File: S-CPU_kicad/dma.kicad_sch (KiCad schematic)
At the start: 31 parts, among them U1 NAND_2, U10 NAND_2, U11 INVERTER_A, U12 INVERTER_A, U13 INVERTER_A, U14 INVERTER_A, U15 NOR_2, U16 DFFR_B, U17 OR_2, U18 NAND_2, U19 DFFR_B, U2 NAND_2, U20 DFFR_B, U21 DFFR_B, U22 NAND_4, U23 NAND_2, U24 INVERTER_A, U25 OR_3, U26 NAND_4, U27 NOR_3, U29 NAND_2, U3 NAND_2, U30 NAND_5, U31 NOR_3, U32 NAND_2, U34 INVERTER_A, U35 NAND_2, U4 NAND_2, U5 NAND_2, U7 NAND_2, U9 NAND_2

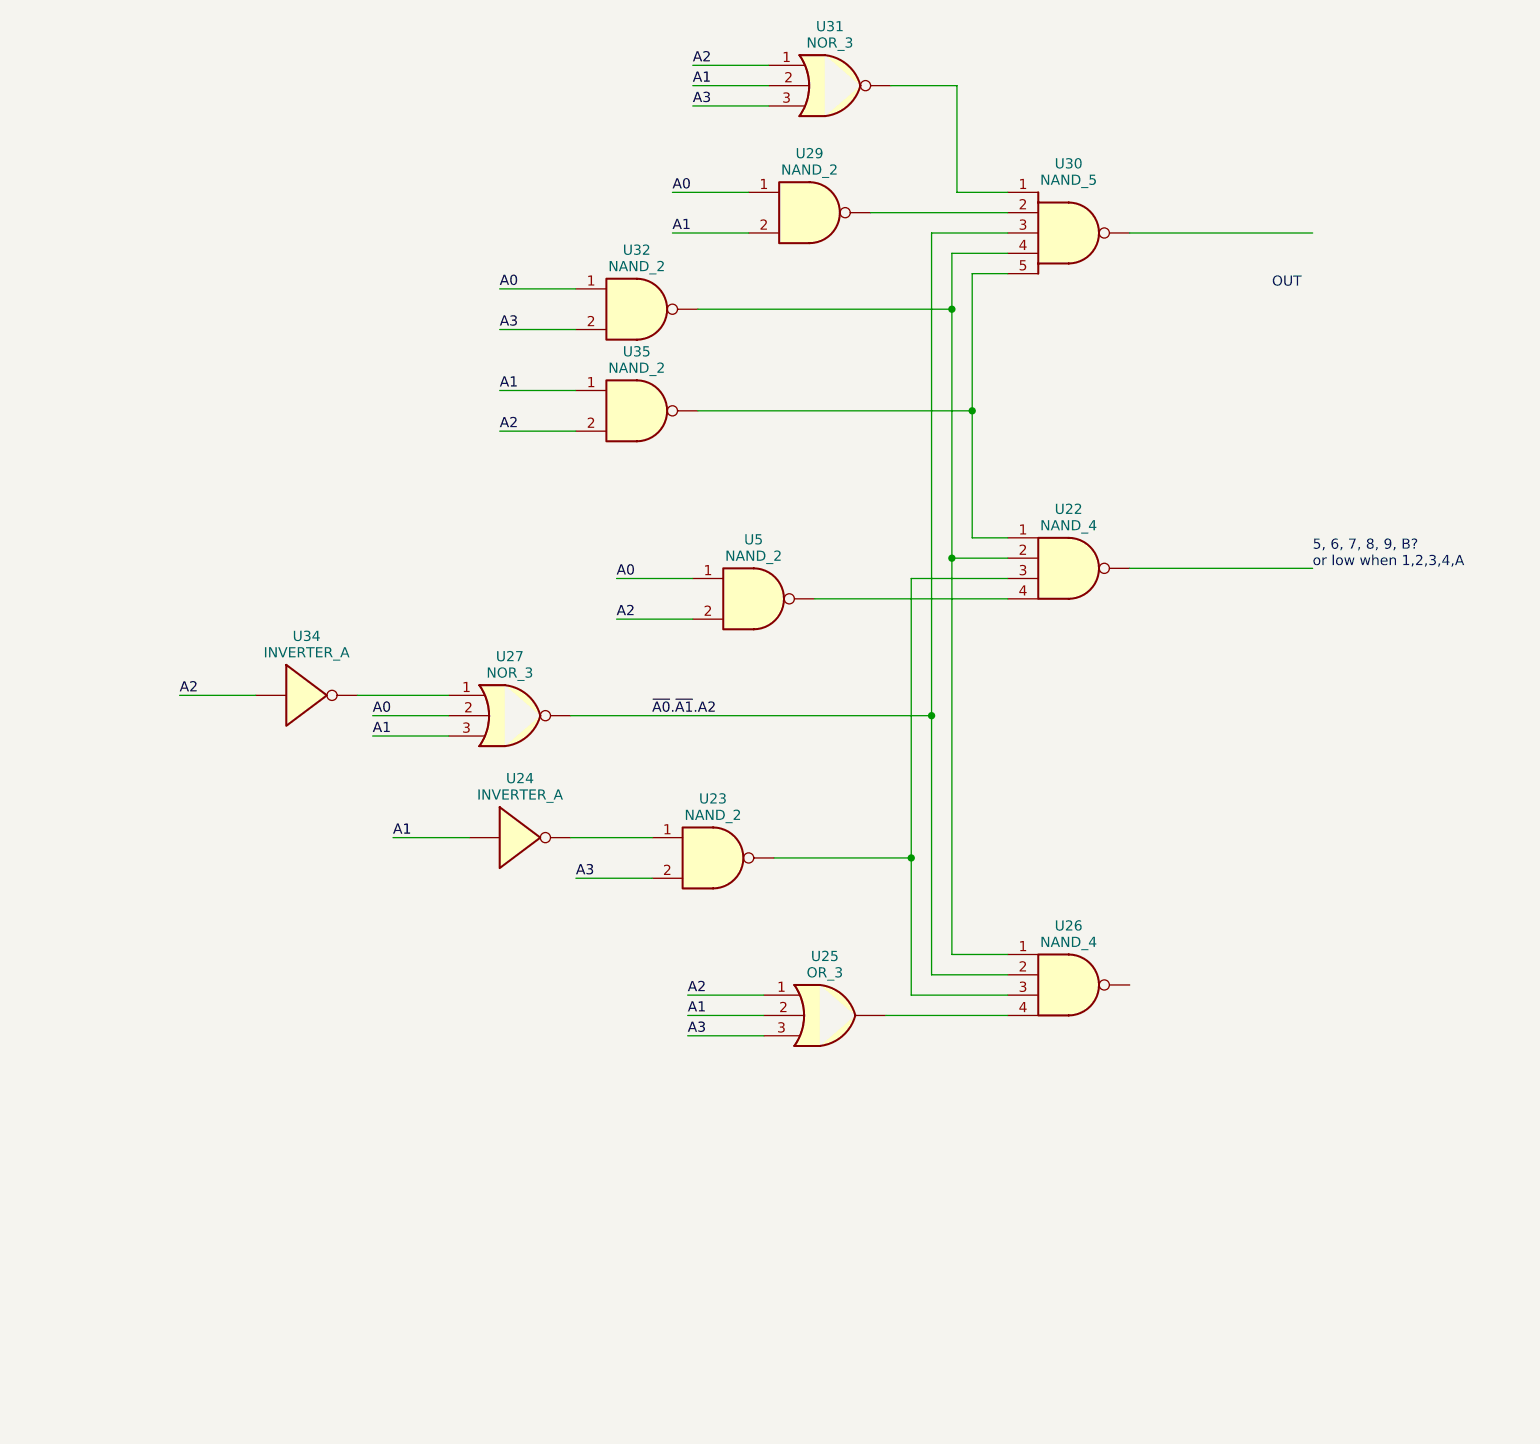
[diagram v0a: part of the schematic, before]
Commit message: Some cells had the wrong ID in the producter remainder sheet. Allocation of new names in spreadsheet for cells in the DMA section
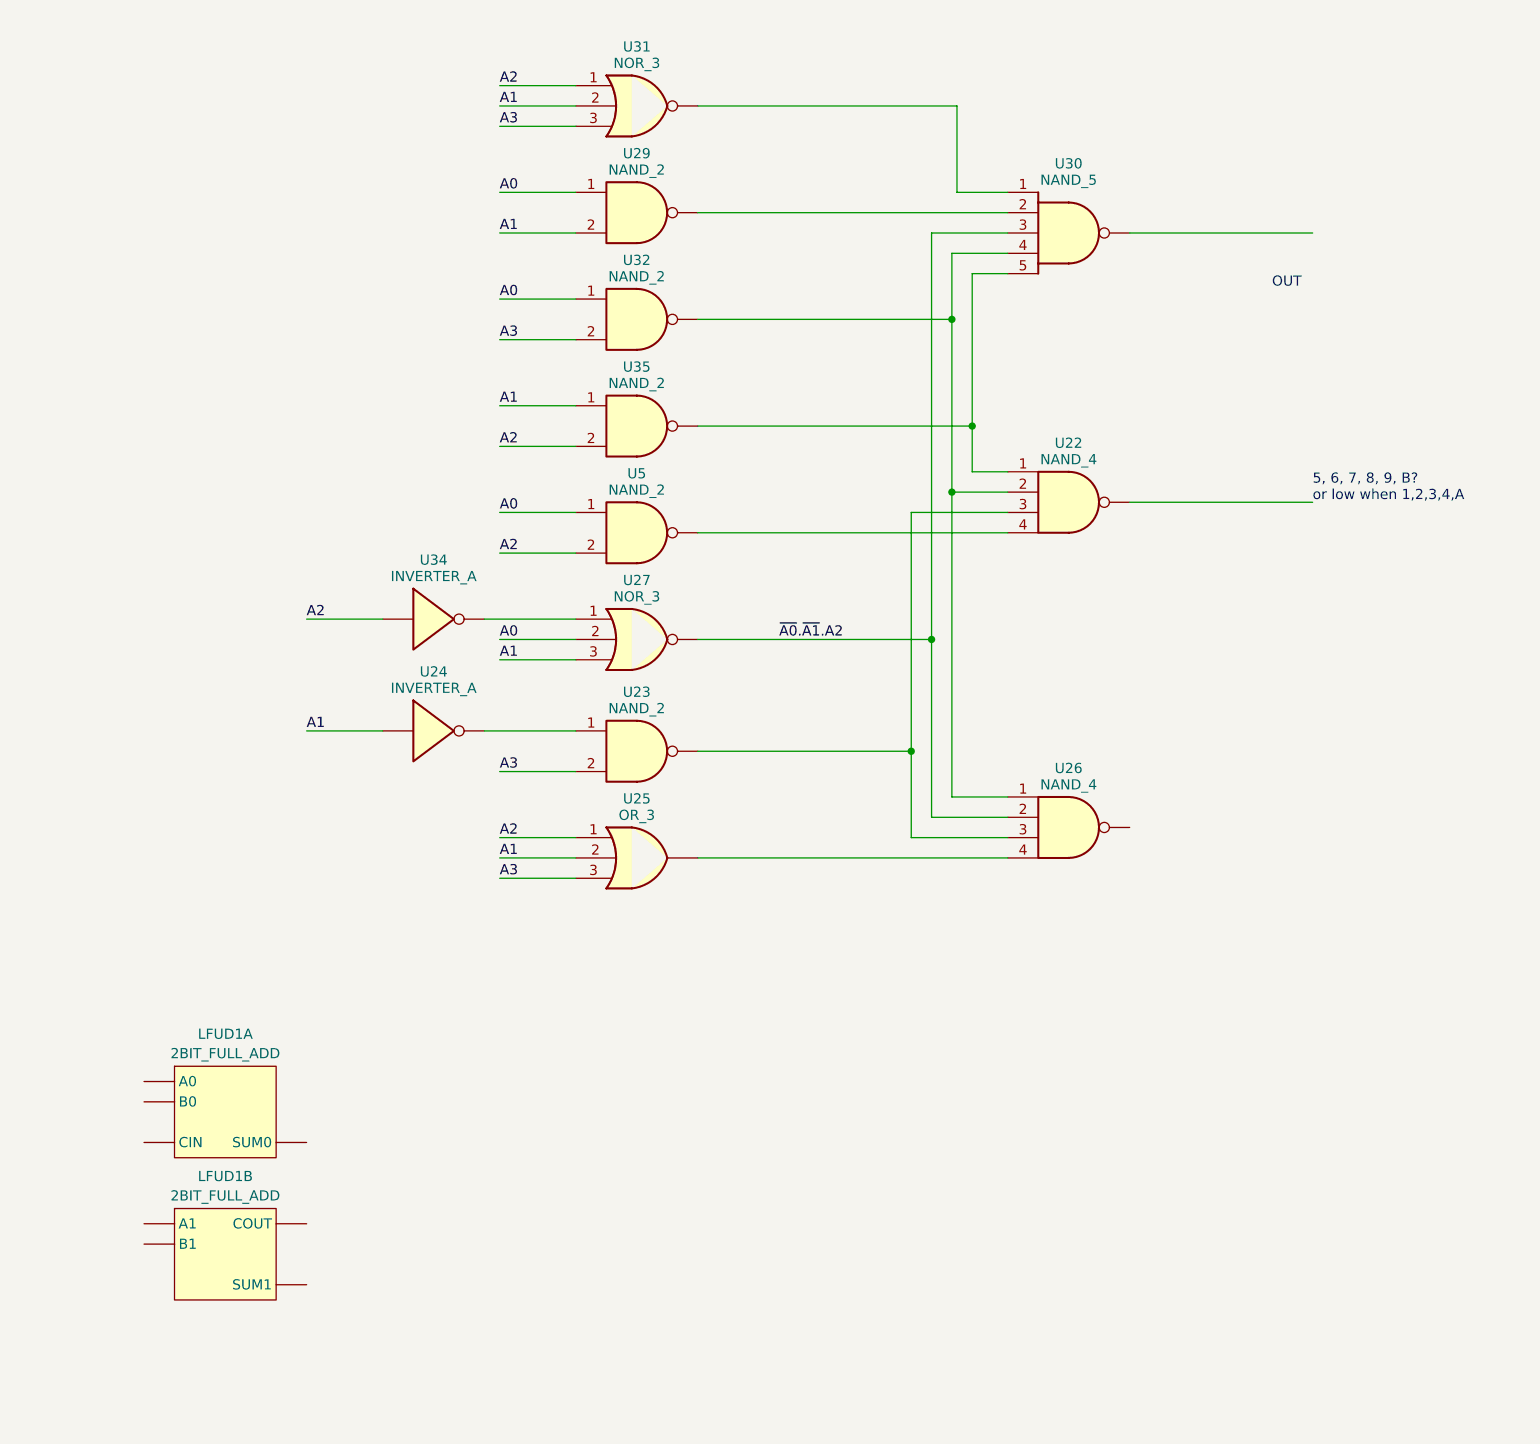
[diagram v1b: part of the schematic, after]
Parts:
- added LFUD1: 2BIT_FULL_ADD, symbol Ricoh_Cells:2BIT_FULL_ADD
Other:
- moved on the sheet: U22, U23, U24, U25, U26, U27, U29, U31, U32, U34, U35, U5

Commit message: Bit DMA section update. Untangled a lot of singals. DMA addressing decoding worked out + connections to DMA RAM.
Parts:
- added AMCK, AMQL: NAND_4, symbol Ricoh_Cells:NAND_4
- added AMEV, AMGY, ANAY, U23, U26, U5: NAND_2, symbol Ricoh_Cells:NAND_2
- added AMEX, AMLH, OKHF (x2), OKPW, OKSL, OKUR, OLCW, OLHT, OLMD, OLOZ, OLRW, OLUQ, OLWK, OMDX, OMMV, QKAT, QKGG, QKLR, RKPQ, RKPR, RKRK, SKPA, TKAS, U22, U24, U25, U27, YKBE: INVERTER_A, symbol Ricoh_Cells:INVERTER_A
- added AMMZ, TKAT: NOR_3, symbol Ricoh_Cells:NOR_3
- added AMZL, DMA?, SKKT, TKAY, TKHG, ULGF, VKDC, VKDV, VKEQ, XKIN, YKCI, YKDI, YKFE, YKHM, YKJS, YKMK: OR_2, symbol Ricoh_Cells:OR_2
- added DMA_RAM_BANK0, DMA_RAM_BANK1, DMA_RAM_BANK2: DMA_RAM, symbol Ricoh_Cells:DMA_RAM
- added EBSG (x2), EBVQ (x2), EBXE (x2), EBYP (x2), ECCU (x2), ECEK (x2), ECGN (x2), ECGO (x2), QKBI, RKNG, SKDA, UKGM, UKGO, UKHI, UKHP, UKOH, UKWD, UKYL (x2): DFFR_A, symbol Ricoh_Cells:DFFR_A
- added OKMN0, OKMN1, OKMN2, OKMN3, OKTR0, OKTR1, OKTR2, OKTR3, OKTY0, OKTY1, OKTY2, OKTY3, OLCO0, OLCO1, OLCO2, OLCO3, OLDU0, OLDU1, OLDU2, OLDU3, OLGV0, OLGV1, OLGV2, OLGV3, OLNC0, OLNC1, OLNC2, OLNC3, OLSH0, OLSH1, OLSH2, OLSH3, OLWI0, OLWI1, OLWI2, OLWI3, OLXX0, OLXX1, OLXX2, OLXX3, OMIG0, OMIG1, OMIG2, OMIG3, OMNC0, OMNC1, OMNC2, OMNC3, QKEL0, QKEL1, QKEL2, QKEL3, QKQM0, QKQM1, QKQM2, QKQM3, RKOE0, RKOE1, RKOE2, RKOE3, RKUL0, RKUL1, RKUL2, RKUL3: TRI_BUF_IF1, symbol Ricoh_Cells:TRI_BUF_IF1
- added OKWN, OLYU, OLZN, OMBB, PKBG, PKEJ, QKAI, SKJF: BUF_DIFF, symbol Ricoh_Cells:BUF_DIFF
- added OLCL0, OLCL1, OLCL2, OLCL3, OLCL4, OLCL5, OLCL6, OLCL7, OLYP0, OLYP1, OLYP2, OLYP3, OLYP4, OLYP5, OLYP6, OLYP7, OLZR0, OLZR1, OLZR2, OLZR3, OLZR4, OLZR5, OLZR6, OLZR7, OMDK0, OMDK1, OMDK2, OMDK3, OMDK4, OMDK5, OMDK6, OMDK7, PKBB0, PKBB1, PKBB2, PKBB3, PKBB4, PKBB5, PKBB6, PKBB7, PKEM0, PKEM1, PKEM2, PKEM3, PKEM4, PKEM5, PKEM6, PKEM7, QKAG0, QKAG1, QKAG2, QKAG3, QKAG4, QKAG5, QKAG6, SKKP0, SKKP1, SKKP2, SKKP3, SKKP4, SKKP5, SKKP6, SKKP7: D_LATCH_ARRAY, symbol Ricoh_Cells:D_LATCH_ARRAY
- added QKAG7, QKAG8, QKAG9, TKGB: DFFR_B, symbol Ricoh_Cells:DFFR_B
- added QKCI, RKMD, RKNZ, SKCS, SKHI, TKBH, TKFI, TKFN, UKZF, ULBK, VKID, VKJK: 2BIT_FULL_ADD, symbol Ricoh_Cells:2BIT_FULL_ADD
- added QKHU, RKQY: NAND_3, symbol Ricoh_Cells:NAND_3
- added RKLP, SKCM, TKIB, TKIB?, U28: AND_2, symbol Ricoh_Cells:AND_2
- added TKDG, WKCF, WKNO, XKGP, XKKB, XKKC, XKKE: OR_3, symbol Ricoh_Cells:OR_3
- added UBNH: NAND_5, symbol Ricoh_Cells:NAND_5
- added VKBO, VKCI, XKBP, XKDB: MUX_2x4:1, symbol Ricoh_Cells:MUX_2x4{colon}1
- added WKSN, WKZC, XKIG, XKQM, YKAW, YKBC, ZKBA, ZKBW: MUX_4x2:1, symbol Ricoh_Cells:MUX_4x2{colon}1
- BNBV: renamed from U31; value NOR_3 -> OR_3; symbol Ricoh_Cells:NOR_3 -> Ricoh_Cells:OR_3
- BNLF: renamed from U27; value NOR_3 -> OR_3; symbol Ricoh_Cells:NOR_3 -> Ricoh_Cells:OR_3
- renumbered U29 to BNAP, U30 to BNHI, U34 to BNNS, U32 to BNOQ, U26 to BNVB, U35 to BNXG, U22 to BNYC, U5 to SKQJ, U24 to ULHH, U23 to ULHM, U25 to VKJX
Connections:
- net A0: now also AMEX.1, AMGY.2, AMMZ.3, AMZL.1, OKHF.1, OKTR3.4, QKQM0.1 (IN), QKQM0.3 (IN)
- net A1: now also AMEV.1, AMLH.1, AMZL.2, ANAY.1, OKHF.1, OKTR2.4, QKQM1.1 (IN), QKQM1.3 (IN); no longer VKJX.2
- net A2: now also AMMZ.2, OKTR1.4, QKQM2.1 (IN), QKQM2.3 (IN), UBNH.2
- net A3: now also ANAY.2, OKTR0.4, QKQM3.1 (IN), QKQM3.3 (IN), UBNH.3
- net at BNVB.3, BNYC.3, ULHM.3: now also AMCK.4
- net ~{A1}+A2+A3: now reaches BNVB.4, VKJX.4
- net at BNVB.5: now also ZKBA.5
- net at ULHH.2, ULHM.1: now also VKJX.2
- net A1+A2+A3: now reaches BNBV.4, BNHI.1
- net at BNHI.6: now also YKCI.2
- net at BNYC.4, SKQJ.3: now also AMCK.3, AMQL.2
- net at BNYC.5: now also ZKBA.13
- net ~{A0}.~{A1}.A2 renamed A0+A1+~{A2}
- new net: RKMD.28 (COUT), SKCS.2 (CIN)
- new net: OLYP2.4 (Q), SKCS.9 (B0)
- new net: VKBO.24, YKAW.13
- new net: OLUQ.2, OLWI0.2 (~{ENA}), OLWI1.2 (~{ENA}), OLWI2.2 (~{ENA}), OLWI3.2 (~{ENA})
- new net: WKZC.7, XKQM.5
- new net: UKHP.1 (~{RESET}), UKHP.5 (~{RESET})
- new net: UKGM.3 (CLK), UKGM.4 (~{CLK}), UKGO.3 (CLK), UKGO.4 (~{CLK}), UKHI.3 (CLK), UKHI.4 (~{CLK}), UKHP.3 (CLK), UKHP.4 (~{CLK}), UKOH.3 (CLK), UKOH.4 (~{CLK}), UKWD.3 (CLK), UKWD.4 (~{CLK}), UKYL.3 (CLK), UKYL.3 (CLK), UKYL.4 (~{CLK}), UKYL.4 (~{CLK}), ULGF.3
- new net: UKHP.6 (Q), VKCI.11
- new net: AMGY.1, AMLH.2, AMMZ.1
- new net: OLGV1.1 (IN), OLGV1.3 (IN)
- new net: OLGV0.2 (~{ENA}), OLGV1.2 (~{ENA}), OLGV2.2 (~{ENA}), OLGV3.2 (~{ENA}), OLHT.2
- new net: RKUL0.1 (IN), RKUL0.3 (IN), SKKP4.4 (Q)
- new net: RKRK.2, RKUL0.2 (~{ENA}), RKUL1.2 (~{ENA}), RKUL2.2 (~{ENA}), RKUL3.2 (~{ENA})
- new net: UKYL.6 (Q), XKBP.11
- new net: EBXE.6 (Q), XKBP.14
- new net: XKBP.24, YKBC.13
- new net: UKGO.1 (~{RESET}), UKGO.5 (~{RESET})
- new net: UKGO.6 (Q), VKBO.11
- new net: UKZF.13 (A0), UKZF.24 (A1), ULBK.13 (A0), ULBK.24 (A1), VKID.13 (A0), VKID.24 (A1), VKJK.13 (A0), VKJK.24 (A1)
- new net: UKZF.28 (COUT), ULBK.2 (CIN)
- new net: OLZR6.4 (Q), ULBK.9 (B0)
- new net: WKCF.4, WKNO.3
- new net: UKZF.2 (CIN), VKJK.28 (COUT)
- new net: OLZR4.4 (Q), UKZF.9 (B0)
- new net: VKCI.24, YKAW.25
- new net: OLYP0.1 (~{ENA}), OLYP1.1 (~{ENA}), OLYP2.1 (~{ENA}), OLYP3.1 (~{ENA}), OLYP4.1 (~{ENA}), OLYP5.1 (~{ENA}), OLYP6.1 (~{ENA}), OLYP7.1 (~{ENA}), OLYU.2
- new net: OLYP0.3 (ENA), OLYP1.3 (ENA), OLYP2.3 (ENA), OLYP3.3 (ENA), OLYP4.3 (ENA), OLYP5.3 (ENA), OLYP6.3 (ENA), OLYP7.3 (ENA), OLYU.2
- new net: OLYP1.4 (Q), RKMD.23 (B1)
- new net: RKUL1.1 (IN), RKUL1.3 (IN), SKKP5.4 (Q)
- new net: OMBB.2, OMDK0.1 (~{ENA}), OMDK1.1 (~{ENA}), OMDK2.1 (~{ENA}), OMDK3.1 (~{ENA}), OMDK4.1 (~{ENA}), OMDK5.1 (~{ENA}), OMDK6.1 (~{ENA}), OMDK7.1 (~{ENA})
- new net: OMBB.2, OMDK0.3 (ENA), OMDK1.3 (ENA), OMDK2.3 (ENA), OMDK3.3 (ENA), OMDK4.3 (ENA), OMDK5.3 (ENA), OMDK6.3 (ENA), OMDK7.3 (ENA)
- new net: OMDK2.4 (Q), TKFN.9 (B0)
- new net: U26.1, U27.2
- new net: U26.3, U28.1
- new net: TKGB.6 (~{Q}), TKHG.1
- new net: TKHG.3, TKIB.2
- new net: SKDA.1 (~{RESET}), SKDA.5 (~{RESET})
- new net: QKAG1.4 (Q), SKDA.2 (D)
- new net: QKAT.2, QKBI.3 (CLK), QKBI.4 (~{CLK}), RKNG.3 (CLK), RKNG.4 (~{CLK}), SKDA.3 (CLK), SKDA.4 (~{CLK})
- new net: OKTY0.2 (~{ENA}), OKTY1.2 (~{ENA}), OKTY2.2 (~{ENA}), OKTY3.2 (~{ENA}), OKUR.2
- new net: OMDK6.4 (Q), RKNZ.9 (B0)
- new net: XKKC.1, XKKE.4
- new net: VKBO.1 (SEL0), VKCI.1 (SEL0), WKSN.1 (SEL), WKZC.1 (SEL), XKBP.1 (SEL0), XKDB.1 (SEL0), XKIG.1 (SEL), XKQM.1 (SEL), YKAW.1 (SEL), YKBC.1 (SEL), YKBE.2, ZKBA.1 (SEL), ZKBW.1 (SEL)
- new net: PKEJ.2, PKEM0.1 (~{ENA}), PKEM1.1 (~{ENA}), PKEM2.1 (~{ENA}), PKEM3.1 (~{ENA}), PKEM4.1 (~{ENA}), PKEM5.1 (~{ENA}), PKEM6.1 (~{ENA}), PKEM7.1 (~{ENA})
- new net: PKEJ.2, PKEM0.3 (ENA), PKEM1.3 (ENA), PKEM2.3 (ENA), PKEM3.3 (ENA), PKEM4.3 (ENA), PKEM5.3 (ENA), PKEM6.3 (ENA), PKEM7.3 (ENA)
- new net: OMIG3.1 (IN), OMIG3.3 (IN), PKEM3.4 (Q)
- new net: OMBB.1, QKAI.1, QKAT.1
- new net: OLNC0.2 (~{ENA}), OLNC1.2 (~{ENA}), OLNC2.2 (~{ENA}), OLNC3.2 (~{ENA}), OLOZ.2
- new net: OLCO1.1 (IN), OLCO1.3 (IN)
- new net: OLCO0.2 (~{ENA}), OLCO1.2 (~{ENA}), OLCO2.2 (~{ENA}), OLCO3.2 (~{ENA}), OLMD.2
- new net: OLRW.2, OLSH0.2 (~{ENA}), OLSH1.2 (~{ENA}), OLSH2.2 (~{ENA}), OLSH3.2 (~{ENA})
- new net: QKGG.1, QKHU.4, QKLR.1
- new net: QKEL0.2 (~{ENA}), QKEL1.2 (~{ENA}), QKEL2.2 (~{ENA}), QKEL3.2 (~{ENA}), QKGG.2
- new net: AMQL.3, ANAY.3
- new net: TKBH.28 (COUT), VKID.2 (CIN)
- new net: OLZR0.4 (Q), VKID.9 (B0)
- new net: RKPR.2, RKQY.1
- new net: OLZN.2, OLZR0.1 (~{ENA}), OLZR1.1 (~{ENA}), OLZR2.1 (~{ENA}), OLZR3.1 (~{ENA}), OLZR4.1 (~{ENA}), OLZR5.1 (~{ENA}), OLZR6.1 (~{ENA}), OLZR7.1 (~{ENA})
- new net: OLZN.2, OLZR0.3 (ENA), OLZR1.3 (ENA), OLZR2.3 (ENA), OLZR3.3 (ENA), OLZR4.3 (ENA), OLZR5.3 (ENA), OLZR6.3 (ENA), OLZR7.3 (ENA)
- new net: OLZR2.4 (Q), VKJK.9 (B0)
- new net: VKBO.29, YKAW.5
- new net: UKGM.6 (Q), VKBO.5
- new net: ECGO.6 (Q), VKBO.8
- new net: ECEK.1 (~{RESET}), ECEK.5 (~{RESET})
- new net: EBSG.3 (CLK), EBSG.4 (~{CLK}), EBVQ.3 (CLK), EBVQ.4 (~{CLK}), EBXE.3 (CLK), EBXE.4 (~{CLK}), EBYP.3 (CLK), EBYP.4 (~{CLK}), ECCU.3 (CLK), ECCU.4 (~{CLK}), ECEK.3 (CLK), ECEK.4 (~{CLK}), ECGN.3 (CLK), ECGN.4 (~{CLK}), ECGO.3 (CLK), ECGO.4 (~{CLK})
- new net: ECEK.6 (Q), VKCI.8
- new net: UKOH.1 (~{RESET}), UKOH.5 (~{RESET})
- new net: UKOH.6 (Q), XKBP.5
- new net: XKKB.1, XKKC.4
- new net: XKIN.1, XKKB.4
- new net: OKHF.2, UBNH.5
- new net: OKMN3.1 (IN), OKMN3.3 (IN), PKBB3.4 (Q)
- new net: OKMN0.2 (~{ENA}), OKMN1.2 (~{ENA}), OKMN2.2 (~{ENA}), OKMN3.2 (~{ENA}), OKPW.2
- new net: WKSN.7, XKIG.5
- new net: SKJF.2, SKKP0.1 (~{ENA}), SKKP1.1 (~{ENA}), SKKP2.1 (~{ENA}), SKKP3.1 (~{ENA}), SKKP4.1 (~{ENA}), SKKP5.1 (~{ENA}), SKKP6.1 (~{ENA}), SKKP7.1 (~{ENA})
- new net: SKKP0.2 (D), TKFI.4 (SUM0)
- new net: SKJF.2, SKKP0.3 (ENA), SKKP1.3 (ENA), SKKP2.3 (ENA), SKKP3.3 (ENA), SKKP4.3 (ENA), SKKP5.3 (ENA), SKKP6.3 (ENA), SKKP7.3 (ENA)
- new net: RKOE0.1 (IN), RKOE0.3 (IN), SKKP0.4 (Q)
- new net: OLYP3.4 (Q), SKCS.23 (B1)
- new net: SKCS.28 (COUT), SKHI.2 (CIN)
- new net: AMQL.1, AMZL.3
- new net: AMQL.5, YKFE.2
- new net: ECGN.6 (Q), VKBO.14
- new net: VKDC.2, YKCI.3, YKDI.1
- new net: YKDI.3, ZKBW.11
- new net: QKAG7.1 (~{RESET}), QKAG7.5 (~{RESET})
- new net: QKAG7.3 (CLK), QKAG7.4 (~{CLK})
- new net: QKAG7.7 (Q), U23.1
- new net: OKWN.2, OLCL0.1 (~{ENA}), OLCL1.1 (~{ENA}), OLCL2.1 (~{ENA}), OLCL3.1 (~{ENA}), OLCL4.1 (~{ENA}), OLCL5.1 (~{ENA}), OLCL6.1 (~{ENA}), OLCL7.1 (~{ENA})
- new net: OKWN.2, OLCL0.3 (ENA), OLCL1.3 (ENA), OLCL2.3 (ENA), OLCL3.3 (ENA), OLCL4.3 (ENA), OLCL5.3 (ENA), OLCL6.3 (ENA), OLCL7.3 (ENA)
- new net: OKTY0.1 (IN), OKTY0.3 (IN), OLCL4.4 (Q)
- new net: QKLR.2, QKQM0.2 (~{ENA}), QKQM1.2 (~{ENA}), QKQM2.2 (~{ENA}), QKQM3.2 (~{ENA})
- new net: QKCI.4 (SUM0), SKKP4.2 (D)
- new net: OKHF.2, UBNH.1
- new net: DMA?.1, UBNH.6
- new net: QKAG0.1 (~{ENA}), QKAG1.1 (~{ENA}), QKAG2.1 (~{ENA}), QKAG3.1 (~{ENA}), QKAG4.1 (~{ENA}), QKAG5.1 (~{ENA}), QKAG6.1 (~{ENA}), QKAI.2
- new net: QKAG0.3 (ENA), QKAG1.3 (ENA), QKAG2.3 (ENA), QKAG3.3 (ENA), QKAG4.3 (ENA), QKAG5.3 (ENA), QKAG6.3 (ENA), QKAI.2
- new net: QKAG8.1 (~{RESET}), QKAG8.5 (~{RESET})
- new net: QKAG8.3 (CLK), QKAG8.4 (~{CLK})
- new net: QKAG8.6 (~{Q}), U5.2
- new net: QKAG8.7 (Q), SKCM.1, TKAT.3, U5.1
- new net: U25.2, ZKBA.16
- new net: OKTR0.1 (IN), OKTR0.3 (IN), PKBB4.4 (Q)
- new net: OKSL.2, OKTR0.2 (~{ENA}), OKTR1.2 (~{ENA}), OKTR2.2 (~{ENA}), OKTR3.2 (~{ENA})
- new net: TKIB?.1, U5.3
- new net: TKIB?.2, U23.3
- new net: UKYL.6 (Q), XKDB.11
- new net: EBSG.6 (Q), XKDB.14
- new net: XKDB.24, YKBC.25
- new net: OMDK1.4 (Q), TKFI.23 (B1)
- new net: RKOE1.1 (IN), RKOE1.3 (IN), SKKP1.4 (Q)
- new net: RKOE0.2 (~{ENA}), RKOE1.2 (~{ENA}), RKOE2.2 (~{ENA}), RKOE3.2 (~{ENA}), RKPQ.2
- new net: OMNC1.1 (IN), OMNC1.3 (IN), PKEM5.4 (Q)
- new net: OMMV.2, OMNC0.2 (~{ENA}), OMNC1.2 (~{ENA}), OMNC2.2 (~{ENA}), OMNC3.2 (~{ENA})
- new net: QKAG3.4 (Q), SKCM.2, TKAS.1
- new net: RKLP.1, SKCM.3
- new net: OKMN0.1 (IN), OKMN0.3 (IN), PKBB0.4 (Q)
- new net: PKBB0.1 (~{ENA}), PKBB1.1 (~{ENA}), PKBB2.1 (~{ENA}), PKBB3.1 (~{ENA}), PKBB4.1 (~{ENA}), PKBB5.1 (~{ENA}), PKBB6.1 (~{ENA}), PKBB7.1 (~{ENA}), PKBG.2
- new net: PKBB0.3 (ENA), PKBB1.3 (ENA), PKBB2.3 (ENA), PKBB3.3 (ENA), PKBB4.3 (ENA), PKBB5.3 (ENA), PKBB6.3 (ENA), PKBB7.3 (ENA), PKBG.2
- new net: OKTR2.1 (IN), OKTR2.3 (IN), PKBB6.4 (Q)
- new net: OMDX.2, OMIG0.2 (~{ENA}), OMIG1.2 (~{ENA}), OMIG2.2 (~{ENA}), OMIG3.2 (~{ENA})
- new net: OMNC0.1 (IN), OMNC0.3 (IN), PKEM4.4 (Q)
- new net: OKTR1.1 (IN), OKTR1.3 (IN), PKBB5.4 (Q)
- new net: OKTR3.1 (IN), OKTR3.3 (IN), PKBB7.4 (Q)
- new net: QKCI.2 (CIN), TKFN.28 (COUT)
- new net: OMDK4.4 (Q), QKCI.9 (B0)
- new net: U24.2, ZKBA.24
- new net: OLWK.2, OLXX0.2 (~{ENA}), OLXX1.2 (~{ENA}), OLXX2.2 (~{ENA}), OLXX3.2 (~{ENA})
- new net: AMEV.2, AMEX.2
- new net: OKMN2.1 (IN), OKMN2.3 (IN), PKBB2.4 (Q)
- new net: TKAT.4, TKAY.1
- new net: OLYP4.4 (Q), SKHI.9 (B0)
- new net: SKKT.2, TKIB.3
- new net: EBVQ.1 (~{RESET}), EBVQ.5 (~{RESET})
- new net: EBVQ.6 (Q), XKDB.8
- new net: SKKP1.2 (D), TKFI.17 (SUM1)
- new net: TKFI.28 (COUT), TKFN.2 (CIN)
- new net: RKOE2.1 (IN), RKOE2.3 (IN), SKKP2.4 (Q)
- new net: EBSG.1 (~{RESET}), EBSG.5 (~{RESET})
- new net: TKAS.2, TKAT.1
- new net: WKZC.20, XKQM.15
- new net: OLCL2.4 (Q), OLDU2.1 (IN), OLDU2.3 (IN)
- new net: OLCW.2, OLDU0.2 (~{ENA}), OLDU1.2 (~{ENA}), OLDU2.2 (~{ENA}), OLDU3.2 (~{ENA})
- new net: OLCO0.1 (IN), OLCO0.3 (IN)
- new net: OLZR1.4 (Q), VKID.23 (B1)
- new net: SKHI.28 (COUT), TKBH.2 (CIN)
- new net: OLYP6.4 (Q), TKBH.9 (B0)
- new net: UKYL.1 (~{RESET}), UKYL.5 (~{RESET}) (x2)
- new net: OLCL0.4 (Q), OLDU0.1 (IN), OLDU0.3 (IN)
- new net: OLCL1.4 (Q), OLDU1.1 (IN), OLDU1.3 (IN)
- new net: QKAG9.1 (~{RESET}), QKAG9.5 (~{RESET})
- new net: QKAG9.3 (CLK), QKAG9.4 (~{CLK})
- new net: QKAG9.7 (Q), U23.2
- new net: RKNG.1 (~{RESET}), RKNG.5 (~{RESET})
- new net: QKAG0.4 (Q), RKNG.2 (D)
- new net: OLZR7.4 (Q), ULBK.23 (B1)
- new net: TKDG.4, WKNO.2
- new net: SKKP3.2 (D), TKFN.17 (SUM1)
- new net: RKOE3.1 (IN), RKOE3.3 (IN), SKKP3.4 (Q)
- new net: OLYP7.4 (Q), TKBH.23 (B1)
- new net: WKNO.4, XKGP.1
- new net: XKGP.2, XKIN.3
- new net: WKSN.9, XKIG.13
- new net: XKDB.29, YKBC.15
- new net: UKWD.6 (Q), XKDB.5
- new net: OKTY3.1 (IN), OKTY3.3 (IN), OLCL7.4 (Q)
- new net: AMCK.2, AMGY.3
- new net: OMNC2.1 (IN), OMNC2.3 (IN), PKEM6.4 (Q)
- new net: WKZC.22, XKQM.25
- new net: OKTY2.1 (IN), OKTY2.3 (IN), OLCL6.4 (Q)
- new net: OLGV3.1 (IN), OLGV3.3 (IN)
- new net: XKBP.29, YKBC.5
- new net: OLGV2.1 (IN), OLGV2.3 (IN)
- new net: OKWN.1, PKBG.1, PKEJ.1
- new net: OMIG1.1 (IN), OMIG1.3 (IN), PKEM1.4 (Q)
- new net: ECGO.1 (~{RESET}), ECGO.5 (~{RESET})
- new net: OLZR5.4 (Q), UKZF.23 (B1)
- new net: VKDV.2, YKFE.3, YKHM.1
- new net: YKHM.3, ZKBW.24
- new net: OMNC3.1 (IN), OMNC3.3 (IN), PKEM7.4 (Q)
- new net: OLCL3.4 (Q), OLDU3.1 (IN), OLDU3.3 (IN)
- new net: OLYP5.4 (Q), SKHI.23 (B1)
- new net: UKGM.1 (~{RESET}), UKGM.5 (~{RESET})
- new net: OMIG0.1 (IN), OMIG0.3 (IN), PKEM0.4 (Q)
- new net: OKMN1.1 (IN), OKMN1.3 (IN), PKBB1.4 (Q)
- new net: EBXE.1 (~{RESET}), EBXE.5 (~{RESET})
- new net: RKPQ.1, RKQY.4, RKRK.1
- new net: TKGB.1 (~{RESET}), TKGB.5 (~{RESET})
- new net: EBYP.1 (~{RESET}), EBYP.5 (~{RESET})
- new net: EBYP.6 (Q), XKBP.8
- new net: QKAG2.4 (Q), QKBI.2 (D)
- new net: UKWD.1 (~{RESET}), UKWD.5 (~{RESET})
- new net: YKMK.3, ZKBW.16
- new net: SKKP2.2 (D), TKFN.4 (SUM0)
- new net: SKKT.1, SKPA.2
- new net: VKEQ.2, YKJS.3, YKMK.1
- new net: QKBI.1 (~{RESET}), QKBI.5 (~{RESET})
- new net: ECGN.1 (~{RESET}), ECGN.5 (~{RESET})
- new net: QKAG4.4 (Q), TKAT.2
- new net: SKJF.1, SKKT.3
- new net: WKSN.22, XKIG.25
- new net: VKID.28 (COUT), VKJK.2 (CIN)
- new net: WKSN.20, XKIG.15
- new net: RKUL3.1 (IN), RKUL3.3 (IN), SKKP7.4 (Q)
- new net: AMCK.1, AMEV.3
- new net: AMCK.5, YKJS.2
- new net: ECCU.1 (~{RESET}), ECCU.5 (~{RESET})
- new net: ECCU.6 (Q), VKCI.14
- new net: U22.2, ZKBW.4
- new net: UKHI.1 (~{RESET}), UKHI.5 (~{RESET})
- new net: UKHI.6 (Q), VKCI.5
- new net: RKUL2.1 (IN), RKUL2.3 (IN), SKKP6.4 (Q)
- new net: OLGV0.1 (IN), OLGV0.3 (IN)
- new net: OMDK3.4 (Q), TKFN.23 (B1)
- new net: OLYP0.4 (Q), RKMD.9 (B0)
- new net: OKTY1.1 (IN), OKTY1.3 (IN), OLCL5.4 (Q)
- new net: QKCI.17 (SUM1), SKKP5.2 (D)
- new net: OMDK5.4 (Q), QKCI.23 (B1)
- new net: QKCI.28 (COUT), RKNZ.2 (CIN)
- new net: OMIG2.1 (IN), OMIG2.3 (IN), PKEM2.4 (Q)
- new net: VKCI.29, YKAW.15
- new net: OMDK0.4 (Q), TKFI.9 (B0)
- new net: RKNZ.4 (SUM0), SKKP6.2 (D)
- new net: OLZR3.4 (Q), VKJK.23 (B1)
- new net: WKZC.9, XKQM.13
- new net: OLCO2.1 (IN), OLCO2.3 (IN)
- new net: OLCO3.1 (IN), OLCO3.3 (IN)
- new net: RKNZ.17 (SUM1), SKKP7.2 (D)
- new net: OMDK7.4 (Q), RKNZ.23 (B1)
- new net +5V: ZKBW.15
- new net 420X: UBNH.4
- new net ??: TKAY.2, TKGB.2 (D), TKHG.2
- new net A0+~{A1}+A2: AMMZ.4, AMQL.4
- new net A10: OMNC1.4
- new net A11: OMNC0.4
- new net A12: OMIG3.4
- new net A13: OMIG2.4
- new net A14: OMIG1.4
- new net A15: OMIG0.4
- new net A16: OKTY3.4
- new net A17: OKTY2.4
- new net A18: OKTY1.4
- new net A19: OKTY0.4
- new net A20: OLDU3.4
- new net A21: OLDU2.4
- new net A22: OLDU1.4
- new net A23: OLDU0.4
- new net A4: OKMN3.4, QKEL0.1 (IN), QKEL0.3 (IN), ZKBW.5
- new net A5: OKMN2.4, QKEL1.1 (IN), QKEL1.3 (IN), ZKBA.25
- new net A6: OKMN1.4, QKEL2.1 (IN), QKEL2.3 (IN), ZKBA.15
- new net A7: OKMN0.4, QKEL3.1 (IN), QKEL3.3 (IN)
- new net A8: OMNC3.4
- new net A9: OMNC2.4
- new net BORROW_FLAG: RKLP.3, RKMD.2 (CIN)
- new net D0: DMA_RAM_BANK1.8 (DIN0), ECGO.2 (D), ECGO.2 (D), OLGV0.4, OLNC0.4, OLXX3.4, VKBO.6, WKSN.4, XKIG.4, YKAW.4
- new net D1: DMA_RAM_BANK1.7 (DIN1), ECGN.2 (D), ECGN.2 (D), OLGV1.4, OLNC1.4, OLXX2.4, VKBO.12, WKSN.11, XKIG.11, YKAW.11
- new net D2: DMA_RAM_BANK1.6 (DIN2), ECEK.2 (D), ECEK.2 (D), OLGV2.4, OLNC2.4, OLXX1.4, VKCI.6, WKSN.16, XKIG.16, YKAW.16
- new net D3: DMA_RAM_BANK1.5 (DIN3), ECCU.2 (D), ECCU.2 (D), OLGV3.4, OLNC3.4, OLXX0.4, VKCI.12, WKSN.24, XKIG.24, YKAW.24
- new net D4: DMA_RAM_BANK1.4 (DIN4), EBYP.2 (D), EBYP.2 (D), OLCO0.4, OLSH0.4, OLWI3.4, WKZC.4, XKBP.6, XKQM.4, YKBC.4
- new net D5: DMA_RAM_BANK1.3 (DIN5), EBXE.2 (D), EBXE.2 (D), OLCO1.4, OLSH1.4, OLWI2.4, WKZC.11, XKBP.12, XKQM.11, YKBC.11
- new net D6: DMA_RAM_BANK1.2 (DIN6), EBVQ.2 (D), EBVQ.2 (D), OLCO2.4, OLSH2.4, OLWI0.4, WKZC.16, XKDB.6, XKQM.16, YKBC.16
- new net D7: DMA_RAM_BANK1.1 (DIN7), EBSG.2 (D), EBSG.2 (D), OLCO3.4, OLSH3.4, OLWI1.4, WKZC.24, XKDB.12, XKQM.24, YKBC.24
- new net DMARAM_A0: DMA_RAM_BANK0.~ (A4), DMA_RAM_BANK1.~ (A4), DMA_RAM_BANK2.~ (A4), ZKBW.7
- new net DMARAM_A1: DMA_RAM_BANK0.~ (A4), DMA_RAM_BANK1.~ (A4), DMA_RAM_BANK2.~ (A4), ZKBA.22
- new net DMARAM_A2: DMA_RAM_BANK0.~ (A4), DMA_RAM_BANK1.~ (A4), DMA_RAM_BANK2.~ (A4), ZKBA.20
- new net DMARAM_A3: DMA_RAM_BANK0.~ (A4), DMA_RAM_BANK2.~ (A4), U28.2, ZKBA.9
- new net DMARAM_A4: DMA_RAM_BANK0.~ (A4), DMA_RAM_BANK1.~ (A4), DMA_RAM_BANK2.~ (A4), U26.2, ZKBA.7
- new net DMARAM_BANK1_A3: DMA_RAM_BANK1.~ (A4), U28.3
- new net DMA_ADDR0: RKMD.4 (SUM0), UKGM.2 (D), VKBO.3, WKCF.1
- new net DMA_ADDR1: RKMD.17 (SUM1), UKGO.2 (D), VKBO.9, WKCF.3
- new net DMA_ADDR10: VKJK.4 (SUM0), WKSN.15, XKKB.2
- new net DMA_ADDR11: VKJK.17 (SUM1), WKSN.25, XKKC.3
- new net DMA_ADDR12: UKZF.4 (SUM0), WKZC.5, XKKC.2
- new net DMA_ADDR13: UKZF.17 (SUM1), WKZC.13, XKKE.3
- new net DMA_ADDR14: ULBK.4 (SUM0), WKZC.15, XKKE.2
- new net DMA_ADDR15: ULBK.17 (SUM1), WKZC.25, XKKE.1
- new net DMA_ADDR2: SKCS.4 (SUM0), UKHI.2 (D), VKCI.3, WKCF.2
- new net DMA_ADDR3: SKCS.17 (SUM1), UKHP.2 (D), VKCI.9, WKNO.1
- new net DMA_ADDR4: SKHI.4 (SUM0), TKDG.3, UKOH.2 (D), XKBP.3
- new net DMA_ADDR5: SKHI.17 (SUM1), TKDG.2, UKYL.2 (D), XKBP.9
- new net DMA_ADDR6: TKBH.4 (SUM0), TKDG.1, UKWD.2 (D), XKDB.3
- new net DMA_ADDR7: TKBH.17 (SUM1), UKYL.2 (D), XKDB.9, XKGP.3
- new net DMA_ADDR8: VKID.4 (SUM0), WKSN.5, XKIN.2
- new net DMA_ADDR9: VKID.17 (SUM1), WKSN.13, XKKB.3
- new net DMA_BANK0_DIN0: DMA_RAM_BANK0.8 (DIN0), YKAW.7
- new net DMA_BANK0_DIN1: DMA_RAM_BANK0.7 (DIN1), YKAW.9
- new net DMA_BANK0_DIN2: DMA_RAM_BANK0.6 (DIN2), YKAW.20
- new net DMA_BANK0_DIN3: DMA_RAM_BANK0.5 (DIN3), YKAW.22
- new net DMA_BANK0_DIN4: DMA_RAM_BANK0.4 (DIN4), YKBC.7
- new net DMA_BANK0_DIN5: DMA_RAM_BANK0.3 (DIN5), YKBC.9
- new net DMA_BANK0_DIN6: DMA_RAM_BANK0.2 (DIN6), YKBC.20
- new net DMA_BANK0_DIN7: DMA_RAM_BANK0.1 (DIN7), YKBC.22
- new net DMA_BANK0_DOUT0: DMA_RAM_BANK0.27 (DOUT0), OLNC0.1 (IN), OLNC0.3 (IN), OLYP0.2 (D), PKBB7.2 (D)
- new net DMA_BANK0_DOUT1: DMA_RAM_BANK0.26 (DOUT1), OLNC1.1 (IN), OLNC1.3 (IN), OLYP1.2 (D), PKBB6.2 (D)
- new net DMA_BANK0_DOUT2: DMA_RAM_BANK0.25 (DOUT2), OLNC2.1 (IN), OLNC2.3 (IN), OLYP2.2 (D), PKBB5.2 (D)
- new net DMA_BANK0_DOUT3: DMA_RAM_BANK0.24 (DOUT3), OLNC3.1 (IN), OLNC3.3 (IN), OLYP3.2 (D), PKBB4.2 (D)
- new net DMA_BANK0_DOUT4: DMA_RAM_BANK0.23 (DOUT4), OLSH0.1 (IN), OLSH0.3 (IN), OLYP4.2 (D), PKBB3.2 (D)
- new net DMA_BANK0_DOUT5: DMA_RAM_BANK0.22 (DOUT5), OLSH1.1 (IN), OLSH1.3 (IN), OLYP5.2 (D), PKBB2.2 (D)
- new net DMA_BANK0_DOUT6: DMA_RAM_BANK0.21 (DOUT6), OLSH2.1 (IN), OLSH2.3 (IN), OLYP6.2 (D), PKBB1.2 (D)
- new net DMA_BANK0_DOUT7: DMA_RAM_BANK0.20 (DOUT7), OLSH3.1 (IN), OLSH3.3 (IN), OLYP7.2 (D), PKBB0.2 (D)
- new net DMA_BANK1_D0: QKAG0.2 (D)
- new net DMA_BANK1_D1: QKAG1.2 (D)
- new net DMA_BANK1_D2: QKAG2.2 (D)
- new net DMA_BANK1_D3: QKAG3.2 (D)
- new net DMA_BANK1_D4: QKAG4.2 (D)
- new net DMA_BANK1_D6: QKAG5.2 (D)
- new net DMA_BANK1_D7: QKAG6.2 (D)
- new net DMA_BANK1_DOUT0: DMA_RAM_BANK1.27 (DOUT0)
- new net DMA_BANK1_DOUT1: DMA_RAM_BANK1.26 (DOUT1)
- new net DMA_BANK1_DOUT2: DMA_RAM_BANK1.25 (DOUT2)
- new net DMA_BANK1_DOUT3: DMA_RAM_BANK1.24 (DOUT3)
- new net DMA_BANK1_DOUT4: DMA_RAM_BANK1.23 (DOUT4)
- new net DMA_BANK1_DOUT5: DMA_RAM_BANK1.22 (DOUT5)
- new net DMA_BANK1_DOUT6: DMA_RAM_BANK1.21 (DOUT6)
- new net DMA_BANK1_DOUT7: DMA_RAM_BANK1.20 (DOUT7)
- new net DMA_BANK2_D0: OMDK0.2 (D)
- new net DMA_BANK2_D1: OMDK1.2 (D)
- new net DMA_BANK2_D2: OMDK2.2 (D)
- new net DMA_BANK2_D3: OMDK3.2 (D)
- new net DMA_BANK2_D4: OMDK4.2 (D)
- new net DMA_BANK2_D5: OMDK5.2 (D)
- new net DMA_BANK2_D6: OMDK6.2 (D)
- new net DMA_BANK2_D7: OMDK7.2 (D)
- new net DMA_BANK2_DIN0: DMA_RAM_BANK2.8 (DIN0), XKIG.7
- new net DMA_BANK2_DIN1: DMA_RAM_BANK2.7 (DIN1), XKIG.9
- new net DMA_BANK2_DIN2: DMA_RAM_BANK2.6 (DIN2), XKIG.20
- new net DMA_BANK2_DIN3: DMA_RAM_BANK2.5 (DIN3), XKIG.22
- new net DMA_BANK2_DIN4: DMA_RAM_BANK2.4 (DIN4), XKQM.7
- new net DMA_BANK2_DIN5: DMA_RAM_BANK2.3 (DIN5), XKQM.9
- new net DMA_BANK2_DIN6: DMA_RAM_BANK2.2 (DIN6), XKQM.20
- new net DMA_BANK2_DIN7: DMA_RAM_BANK2.1 (DIN7), XKQM.22
- new net DMA_BANK2_DOUT0: DMA_RAM_BANK2.27 (DOUT0), OLXX3.1 (IN), OLXX3.3 (IN), OLZR0.2 (D), PKEM7.2 (D)
- new net DMA_BANK2_DOUT1: DMA_RAM_BANK2.26 (DOUT1), OLXX2.1 (IN), OLXX2.3 (IN), OLZR1.2 (D), PKEM6.2 (D)
- new net DMA_BANK2_DOUT2: DMA_RAM_BANK2.25 (DOUT2), OLXX1.1 (IN), OLXX1.3 (IN), OLZR2.2 (D), PKEM5.2 (D)
- new net DMA_BANK2_DOUT3: DMA_RAM_BANK2.24 (DOUT3), OLXX0.1 (IN), OLXX0.3 (IN), OLZR3.2 (D), PKEM4.2 (D)
- new net DMA_BANK2_DOUT4: DMA_RAM_BANK2.23 (DOUT4), OLWI3.1 (IN), OLWI3.3 (IN), OLZR4.2 (D), PKEM3.2 (D)
- new net DMA_BANK2_DOUT5: DMA_RAM_BANK2.22 (DOUT5), OLWI2.1 (IN), OLWI2.3 (IN), OLZR5.2 (D), PKEM2.2 (D)
- new net DMA_BANK2_DOUT6: DMA_RAM_BANK2.21 (DOUT6), OLWI0.1 (IN), OLWI0.3 (IN), OLZR6.2 (D), PKEM1.2 (D)
- new net DMA_BANK2_DOUT7: DMA_RAM_BANK2.20 (DOUT7), OLWI1.1 (IN), OLWI1.3 (IN), OLZR7.2 (D), PKEM0.2 (D)
- new net DMA_CHAN0: U22.1
- new net DMA_CHAN1: U24.1
- new net DMA_CHAN2: U25.1
- new net DMA_CLK?: U27.1, YKBE.1
- new net GND: QKCI.13 (A0), QKCI.24 (A1), RKNZ.13 (A0), RKNZ.24 (A1), TKFI.2 (CIN), TKFN.13 (A0), TKFN.24 (A1)
- new net PA0: QKQM0.4, RKOE0.4
- new net PA1: QKQM1.4, RKOE1.4
- new net PA2: QKQM2.4, RKOE2.4
- new net PA3: QKQM3.4, RKOE3.4
- new net PA4: QKEL0.4, RKUL0.4
- new net PA5: QKEL1.4, RKUL1.4
- new net PA6: QKEL2.4, RKUL2.4
- new net PA7: QKEL3.4, RKUL3.4
- new net wDBJW_wHASI_RST: EBSG.1 (~{RESET}), EBSG.5 (~{RESET}), EBVQ.1 (~{RESET}), EBVQ.5 (~{RESET}), EBXE.1 (~{RESET}), EBXE.5 (~{RESET}), EBYP.1 (~{RESET}), EBYP.5 (~{RESET}), ECCU.1 (~{RESET}), ECCU.5 (~{RESET}), ECEK.1 (~{RESET}), ECEK.5 (~{RESET}), ECGN.1 (~{RESET}), ECGN.5 (~{RESET}), ECGO.1 (~{RESET}), ECGO.5 (~{RESET})
- new net wJBQK: OKPW.1, OKSL.1, OKUR.1, OLCW.1, OMDX.1, OMMV.1, QKHU.1, RKPR.1
- new net wNBBM_wNAQE_XIN/2: TKIB.1
- new net wNBKW_wNBPG_XIN/4: OLYU.1, OLZN.1
- new net wOAFI_wOACU_XIN/4: ULGF.1
- new net wOBXZ_wOCHV_XIN/2: TKGB.3 (CLK), TKGB.4 (~{CLK})
- new net wQKAG5: QKAG5.4 (Q)
- new net wQKBI: QKBI.6 (Q), VKBO.20 (SEL1), VKCI.20 (SEL1), XKBP.20 (SEL1), XKDB.20 (SEL1)
- new net wRKNG: RKNG.6 (Q)
- new net wSKDA: SKDA.6 (Q)
- new net ~{420C_WR}: DMA?.3, EBSG.3 (CLK), EBSG.4 (~{CLK}), EBVQ.3 (CLK), EBVQ.4 (~{CLK}), EBXE.3 (CLK), EBXE.4 (~{CLK}), EBYP.3 (CLK), EBYP.4 (~{CLK}), ECCU.3 (CLK), ECCU.4 (~{CLK}), ECEK.3 (CLK), ECEK.4 (~{CLK}), ECGN.3 (CLK), ECGN.4 (~{CLK}), ECGO.3 (CLK), ECGO.4 (~{CLK})
- new net ~{4300-437F}: YKCI.1, YKFE.1, YKJS.1
- new net ~{DMA_BANK0_RD}: OLOZ.1, OLRW.1, VKDC.3
- new net ~{DMA_BANK0_WR}: DMA_RAM_BANK0.17 (WR), ZKBW.9
- new net ~{DMA_BANK1_RD}: OLHT.1, OLMD.1, VKEQ.3
- new net ~{DMA_BANK1_WR}: DMA_RAM_BANK1.17 (WR), ZKBW.20
- new net ~{DMA_BANK2_RD}: OLUQ.1, OLWK.1, VKDV.3
- new net ~{DMA_BANK2_WR}: DMA_RAM_BANK2.17 (WR), ZKBW.22
- new net ~{DMA_RD}: VKDC.1, VKDV.1, VKEQ.1
- new net ~{DMA_WR}: YKDI.2, YKHM.2, YKMK.2
- new net ~{INC}_DEC: RKLP.2, RKMD.13 (A0), RKMD.24 (A1), SKCS.13 (A0), SKCS.24 (A1), SKHI.13 (A0), SKHI.24 (A1), TKAY.3, TKBH.13 (A0), TKBH.24 (A1)
- new net ~{MODE5}: QKHU.3, RKQY.3, SKPA.1
- new net ~{MODE6}: QKHU.2, RKQY.2
- no-connect marks 0 -> 22
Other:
- note added: "A0 0 1 0 1 0 1 0 1 0 1 0 1 0 1 0 1"
- note added: "A1 0 0 1 1 0 0 1 1 0 0 1 1 0 0 1 1"
- note added: "A2 0 0 0 0 1 1 1 1 0 0 0 0 1 1 1 1"
- note added: "A3 0 0 0 0 0 0 0 0 1 1 1 1 1 1 1 1"
- note added: "AMCK B1_ENB 0 1 1 1 0 1 1 0 1 1 1 0 x x x 0"
- note added: "AMQL B2_ENB 1 0 1 0 1 1 0 1 1 0 1 1 x x x 1"
- note added: "A_BUS Address coming from DMA banks"
- note added: "BANK0_ENB, low when A3-0 = 2,5,8,A BNHI = 000x + xx11 + x100 + 1xx1 + x11x"
- note added: "BANK1_ENB, low when A3-0 = 0,4,7,B,F AMCK = xx10 + xx01 + 1x0x + 001x"
- note added: "BANK2_ENB, low when A3-0 = 1,3,6,9 AMQL = xx00 + x1x1 + 1x1x + x010"
- note added: "BMHI B0_ENB 1 1 0 1 1 0 1 1 0 1 0 1 x x x 1"
- note added: "BNVB A4 0 0 1 1 1 0 0 0 1 1 0 1 x x x 1"
- note added: "BNVB_A4 is low when 0,1,5,6,7,A BNVB = 1xx1 + x100 + 1x0x + 001x"
- note added: "BNYC A3 0 0 0 0 0 1 1 1 1 1 0 1 x x x 1"
- note added: "BNYC_A3 is low when 0,1,2,3,4,A BNYC = x11x + 1xx1 + 1x0x + x1x1"
- note added: "B_BUS Address coming from DMA banks during DMA or from A bus otherwise"
- note added: "Bank 1 data not altered during DMA transfer unlike bank 0 and 2"
- note added: "DMA RAM control signals decoding"
- note added: "DMA Registers Parameters for DMA Transfer B Address A Address (Low Byte) A Address (High Byte) A Address Bank Number Bytes to Transfer (Low Byte) (DMA) Number Bytes to Transfer (High Byte) (DMA) Data Bank (H-DMA) A2 Table Address (Low Byte) A2 Table Address (High Byte) Number of Lines to Transfer (H-DMA) Fast Access memory x x x Fast Access memory mirror"
- note added: "JBQK = '0' when DMA is active"
- note removed: "5, 6, 7, 8, 9, B? or low when 1,2,3,4,A"
- note removed: "OUT"
- moved on the sheet: BNAP, BNHI, BNNS, BNOQ, BNVB, BNXG, BNYC, LFUD1A, LFUD1B, SKQJ, U1, U10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

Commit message: NOR SR latch identified.
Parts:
- removed DMA?: OR_2, symbol Ricoh_Cells:OR_2
- removed EBSG, EBVQ, EBXE, EBYP, ECCU, ECEK, ECGN, ECGO: DFFR_A, symbol Ricoh_Cells:DFFR_A
- removed OKHF (x2): INVERTER_A, symbol Ricoh_Cells:INVERTER_A
- removed UBNH: NAND_5, symbol Ricoh_Cells:NAND_5
- added RKMW: NOR_8, symbol Ricoh_Cells:NOR_8
- added SKDK: INVERTER_A, symbol Ricoh_Cells:INVERTER_A
- renumbered U26 to SKCA, U28 to TKAC, U27 to UKBI
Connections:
- net D0: now also RKMW.1
- net D1: now also RKMW.2
- net D2: now also RKMW.3
- net D3: now also RKMW.4
- net D4: now also RKMW.5
- net D5: now also RKMW.6
- net D6: now also RKMW.7
- net D7: now also RKMW.8
- new net: RKMW.9, SKDK.1
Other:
- added sheet DMA Logic (dmalogic.kicad_sch)

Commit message: Further updates in the DMA region. SYS clock identified at last!
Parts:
- removed U1, U7: NAND_2, symbol Ricoh_Cells:NAND_2
- added PORZ, RKMU, SKDK?, XKGY, YKQD: INVERTER_A, symbol Ricoh_Cells:INVERTER_A
- added POSD, TKIB?: AND_2, symbol Ricoh_Cells:AND_2
- added RKUL4: TRI_BUF_IF1, symbol Ricoh_Cells:TRI_BUF_IF1
- added U1: NOR_2, symbol Ricoh_Cells:NOR_2
- added YKMY: BUF, symbol Ricoh_Cells:BUF
- added YKNB, YKOE: DELAY_BUF, symbol Ricoh_Cells:DELAY_BUF
- TKAT: value NOR_3 -> AND_3; symbol Ricoh_Cells:NOR_3 -> Ricoh_Cells:AND_3
- renumbered QKAG8 to POSI
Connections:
- net A4: now also ZKBA.15; no longer ZKBW.5
- net A6: now also ZKBW.5; no longer ZKBA.15
- net DMARAM_A0: now also SKCA.2, ZKBA.7; no longer ZKBW.7
- net DMARAM_A1: now also TKAC.2, ZKBA.9; no longer ZKBA.22
- net DMARAM_A3: now also ZKBA.22; no longer TKAC.2, ZKBA.9
- net DMARAM_A4: now also ZKBW.7; no longer SKCA.2, ZKBA.7
- net DMA_CHAN0: now also U25.1; no longer U22.1
- net DMA_CHAN2: now also U22.1; no longer U25.1
- net DMA_CLK?: no longer YKBE.1
- net PA4: now also RKUL4.4
- net wQKAG5: now also RKMU.1
- net ~{MODE5}: now also RKUL4.2 (~{ENA})
- net at VKBO.1 (SEL0), VKCI.1 (SEL0), XKBP.1 (SEL0)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: no longer WKSN.1 (SEL), WKZC.1 (SEL)
- net at POSI.7 (Q), U5.1: no longer SKCM.1, TKAT.3
- net wQKAG3: now reaches QKAG3.4 (Q), SKCM.2, TKAS.1
- net at WKNO.4, XKGP.1: now also XKGY.1
- net at XKGP.4: now also U1.2
- net at TKAT.2: now also SKCM.1, POSD.3; no longer QKAG4.4 (Q)
- net at SKDK.2: now also SKDK?.1
- net ?? renamed wNBEG_wNBEB_XIN/8
- new net: YKOE.2, YKQD.1
- new net: RKUL4.1 (IN), RKUL4.3 (IN), XKGY.2
- new net: PORZ.2, POSD.1
- new net: WKSN.1 (SEL), WKZC.1 (SEL), YKMY.2
- new net: YKMY.1, YKNB.2
- new net: QKAG4.4 (Q), TKAT.3
- new net: SKDK?.2, TKIB?.1
- new net DMA_OFF: YKBE.1
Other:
- sheet DMA Logic renamed DMA & HDMA Control Registers
- added sheet Other DMA gates (DMAothers.kicad_sch)
- sheet DMA & HDMA Control Registers ports: added 420X, A[0..15], DMA_CHAN[0..2], D[0..7], RISING_VBLANK, wNBEG_wNBEB_XIN/8, ~{DMA_WR}, ~{NO_DMA}, ~{NO_HDMA}; removed none
- note added: "0= INC or DEC, 1= Fixed"
- note added: "0= INC, 1= DEC"
- note added: "DMA RAM control signals decoding (Registers 43x0-43xF)"
- note removed: "DMA RAM control signals decoding"
- moved on the sheet: LFUD1A, LFUD1B, POSI, QKAG7, QKAG9, RKLP, SKCA, SKCM, TKAC, TKAS, TKAY, TKIB?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
